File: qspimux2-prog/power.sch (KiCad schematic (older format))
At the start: 11 parts, among them Q601 BSS138, U601 MIC5504-3.3YM5, U602 AP2127K-ADJ

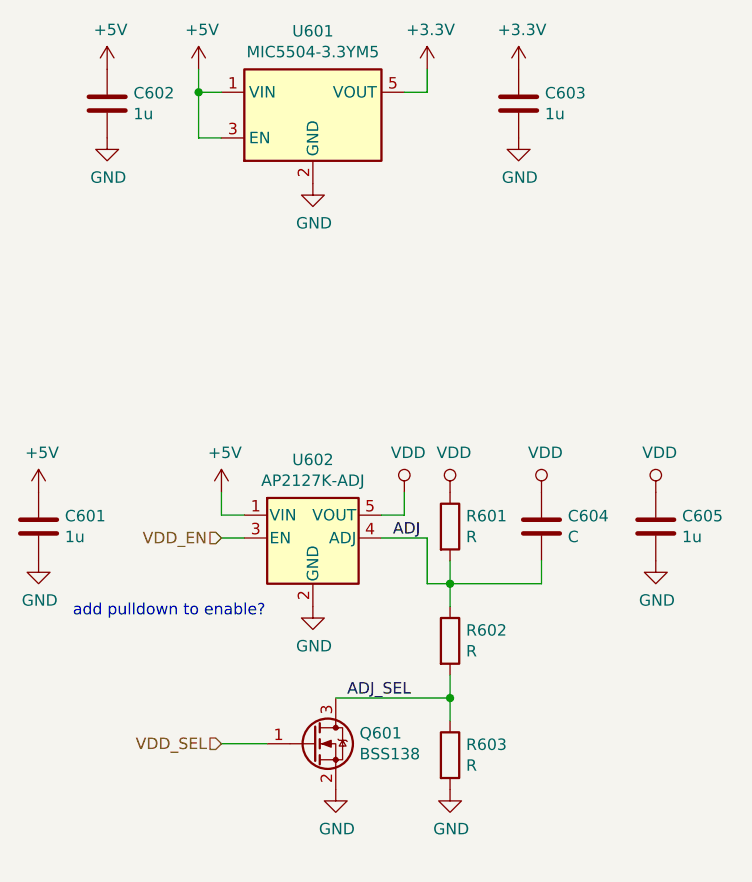
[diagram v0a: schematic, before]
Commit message: qspimux2-prog: add pull down resistors to enable and select inputs of vdd regulator
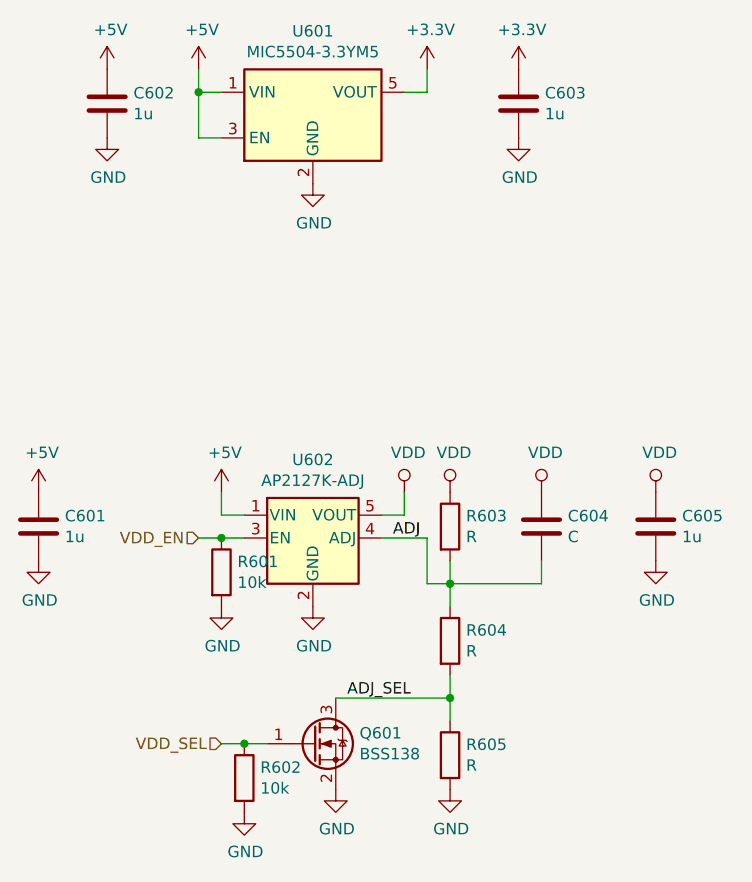
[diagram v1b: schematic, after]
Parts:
- added R601, R602: 10k, Resistor_SMD:R_0402_1005Metric, symbol Device:R
- renumbered R601 to R603, R602 to R604, R603 to R605
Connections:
- net GND: now also R601.2, R602.2
- net VDD_EN: now also R601.1
- net VDD_SEL: now also R602.1
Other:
- note removed: "add pulldown to enable?"
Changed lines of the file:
@@
 $EndComp
 $Comp
-L power:+3.3V #PWR0614
+L power:+3.3V #PWR0616
 U 1 1 5E022EF0
 P 3900 2550
-F 0 "#PWR0614" H 3900 2400 50  0001 C CNN
+F 0 "#PWR0616" H 3900 2400 50  0001 C CNN
 F 1 "+3.3V" H 3915 2723 50  0000 C CNN
 F 2 "" H 3900 2550 50  0001 C CNN
@@
 $EndComp
 $Comp
-L power:+3.3V #PWR0611
+L power:+3.3V #PWR0613
 U 1 1 5E0224B7
 P 3500 2550
-F 0 "#PWR0611" H 3500 2400 50  0001 C CNN
+F 0 "#PWR0613" H 3500 2400 50  0001 C CNN
 F 1 "+3.3V" H 3515 2723 50  0000 C CNN
 F 2 "" H 3500 2550 50  0001 C CNN
@@
 $EndComp
 $Comp
-L power:GND #PWR0607
+L power:GND #PWR0609
 U 1 1 5E020A11
 P 3000 3050
-F 0 "#PWR0607" H 3000 2800 50  0001 C CNN
+F 0 "#PWR0609" H 3000 2800 50  0001 C CNN
 F 1 "GND" H 3005 2877 50  0000 C CNN
 F 2 "" H 3000 3050 50  0001 C CNN
@@
 $EndComp
 $Comp
-L power:GND #PWR0615
+L power:GND #PWR0617
 U 1 1 5E021D81
 P 3900 2850
-F 0 "#PWR0615" H 3900 2600 50  0001 C CNN
+F 0 "#PWR0617" H 3900 2600 50  0001 C CNN
 F 1 "GND" H 3905 2677 50  0000 C CNN
 F 2 "" H 3900 2850 50  0001 C CNN
@@
 VDD_SEL
 $Comp
-L power:VDD #PWR0617
+L power:VDD #PWR0619
 U 1 1 5DF779E9
 P 4500 4400
-F 0 "#PWR0617" H 4500 4250 50  0001 C CNN
+F 0 "#PWR0619" H 4500 4250 50  0001 C CNN
 F 1 "VDD" H 4517 4573 50  0000 C CNN
 F 2 "" H 4500 4400 50  0001 C CNN
@@
 	1    0    0    -1
 $EndComp
-Text HLabel 2600 4600 0    50   Input ~ 0
+Text HLabel 2500 4600 0    50   Input ~ 0
 VDD_EN
 $Comp
-L power:GND #PWR0608
+L power:GND #PWR0610
 U 1 1 5DED5ED3
 P 3000 4900
-F 0 "#PWR0608" H 3000 4650 50  0001 C CNN
+F 0 "#PWR0610" H 3000 4650 50  0001 C CNN
 F 1 "GND" H 3005 4727 50  0000 C CNN
 F 2 "" H 3000 4900 50  0001 C CNN
@@
 $EndComp
 $Comp
-L power:GND #PWR0618
+L power:GND #PWR0620
 U 1 1 5DED62F9
 P 4500 4700
-F 0 "#PWR0618" H 4500 4450 50  0001 C CNN
+F 0 "#PWR0620" H 4500 4450 50  0001 C CNN
 F 1 "GND" H 4505 4527 50  0000 C CNN
 F 2 "" H 4500 4700 50  0001 C CNN
@@
 $EndComp
 $Comp
-L power:VDD #PWR0610
+L power:VDD #PWR0612
 U 1 1 5DED7A92
 P 3400 4400
-F 0 "#PWR0610" H 3400 4250 50  0001 C CNN
+F 0 "#PWR0612" H 3400 4250 50  0001 C CNN
 F 1 "VDD" H 3417 4573 50  0000 C CNN
 F 2 "" H 3400 4400 50  0001 C CNN
@@
 $EndComp
 $Comp
-L Device:R R601
+L Device:R R603
 U 1 1 5DEEFCBB
 P 3600 4550
-F 0 "R601" H 3670 4596 50  0000 L CNN
+F 0 "R603" H 3670 4596 50  0000 L CNN
 F 1 "R" H 3670 4505 50  0000 L CNN
 F 2 "Resistor_SMD:R_0402_1005Metric" V 3530 4550 50  0001 C CNN
@@
 $EndComp
 $Comp
-L Device:R R602
+L Device:R R604
 U 1 1 5DEF0794
 P 3600 5050
-F 0 "R602" H 3670 5096 50  0000 L CNN
+F 0 "R604" H 3670 5096 50  0000 L CNN
 F 1 "R" H 3670 5005 50  0000 L CNN
 F 2 "Resistor_SMD:R_0402_1005Metric" V 3530 5050 50  0001 C CNN
@@
 $EndComp
 $Comp
-L Device:R R603
+L Device:R R605
 U 1 1 5DEF5357
 P 3600 5550
-F 0 "R603" H 3670 5596 50  0000 L CNN
+F 0 "R605" H 3670 5596 50  0000 L CNN
 F 1 "R" H 3670 5505 50  0000 L CNN
 F 2 "Resistor_SMD:R_0402_1005Metric" V 3530 5550 50  0001 C CNN
@@
 $EndComp
 $Comp
-L power:GND #PWR0613
+L power:GND #PWR0615
 U 1 1 5DEF7FD0
 P 3600 5700
-F 0 "#PWR0613" H 3600 5450 50  0001 C CNN
+F 0 "#PWR0615" H 3600 5450 50  0001 C CNN
 F 1 "GND" H 3605 5527 50  0000 C CNN
 F 2 "" H 3600 5700 50  0001 C CNN
@@
 	3400 4500 3400 4400
 $Comp
-L power:VDD #PWR0612
+L power:VDD #PWR0614
 U 1 1 5DEFBE7B
 P 3600 4400
-F 0 "#PWR0612" H 3600 4250 50  0001 C CNN
+F 0 "#PWR0614" H 3600 4250 50  0001 C CNN
 F 1 "VDD" H 3617 4573 50  0000 C CNN
 F 2 "" H 3600 4400 50  0001 C CNN
@@
 	4000 4800 4000 4700
 $Comp
-L power:VDD #PWR0616
+L power:VDD #PWR0618
 U 1 1 5DF067EF
 P 4000 4400
-F 0 "#PWR0616" H 4000 4250 50  0001 C CNN
+F 0 "#PWR0618" H 4000 4250 50  0001 C CNN
 F 1 "VDD" H 4017 4573 50  0000 C CNN
 F 2 "" H 4000 4400 50  0001 C CNN
@@
 	3600 5300 3600 5200
 $Comp
-L power:GND #PWR0609
+L power:GND #PWR0611
 U 1 1 5DF0FC05
 P 3100 5700
-F 0 "#PWR0609" H 3100 5450 50  0001 C CNN
+F 0 "#PWR0611" H 3100 5450 50  0001 C CNN
 F 1 "GND" H 3105 5527 50  0000 C CNN
 F 2 "" H 3100 5700 50  0001 C CNN
@@
 ADJ_SEL
 Wire Wire Line
+	2500 4600 2600 4600
+Wire Wire Line
+	2600 5500 2700 5500
+$Comp
+L Device:R R602
+U 1 1 5DED3942
+P 2700 5650
+F 0 "R602" H 2770 5696 50  0000 L CNN
+F 1 "10k" H 2770 5605 50  0000 L CNN
+F 2 "Resistor_SMD:R_0402_1005Metric" V 2630 5650 50  0001 C CNN
+F 3 "~" H 2700 5650 50  0001 C CNN
+	1    2700 5650
+	1    0    0    -1
+$EndComp
+Connection ~ 2700 5500
+Wire Wire Line
+	2700 5500 2800 5500
+$Comp
+L power:GND #PWR0608
+U 1 1 5DEDC3EC
+P 2700 5800
+F 0 "#PWR0608" H 2700 5550 50  0001 C CNN
+F 1 "GND" H 2705 5627 50  0000 C CNN
+F 2 "" H 2700 5800 50  0001 C CNN
+F 3 "" H 2700 5800 50  0001 C CNN
+	1    2700 5800
+	1    0    0    -1
+$EndComp
+$Comp
+L Device:R R601
+U 1 1 5DEE2184
+P 2600 4750
+F 0 "R601" H 2670 4796 50  0000 L CNN
+F 1 "10k" H 2670 4705 50  0000 L CNN
+F 2 "Resistor_SMD:R_0402_1005Metric" V 2530 4750 50  0001 C CNN
+F 3 "~" H 2600 4750 50  0001 C CNN
+	1    2600 4750
+	1    0    0    -1
+$EndComp
+Connection ~ 2600 4600
+Wire Wire Line
 	2600 4600 2700 4600
-Text Notes 1950 4950 0    50   ~ 0
-add pulldown to enable?
-Wire Wire Line
-	2600 5500 2800 5500
+$Comp
+L power:GND #PWR0607
+U 1 1 5DEE6044
+P 2600 4900
+F 0 "#PWR0607" H 2600 4650 50  0001 C CNN
+F 1 "GND" H 2605 4727 50  0000 C CNN
+F 2 "" H 2600 4900 50  0001 C CNN
+F 3 "" H 2600 4900 50  0001 C CNN
+	1    2600 4900
+	1    0    0    -1
+$EndComp
 $EndSCHEMATC

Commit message: qspimux2-prog: add values for ldo feedback network
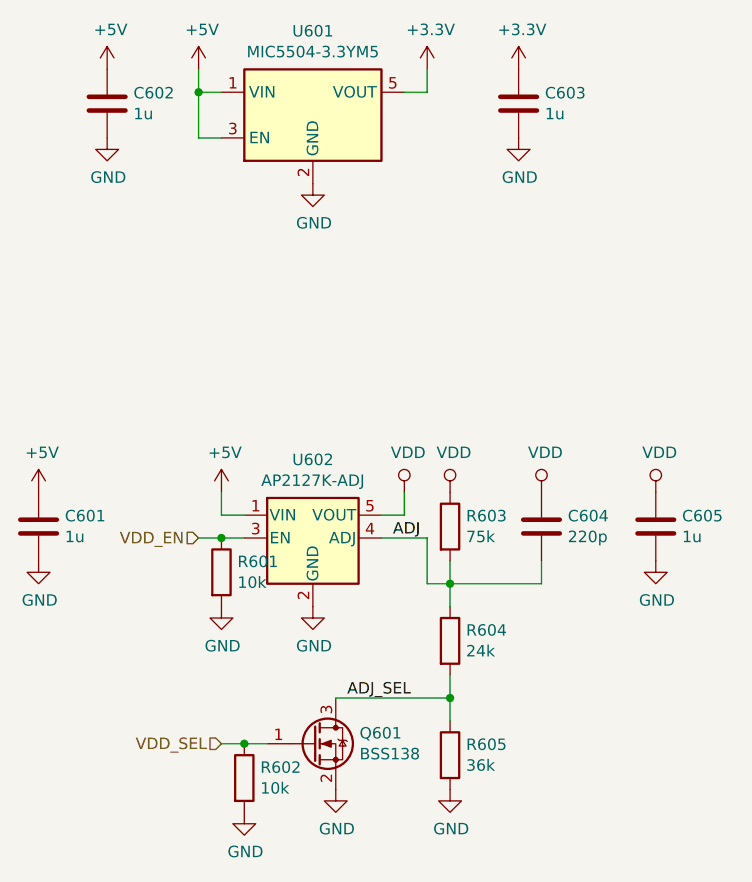
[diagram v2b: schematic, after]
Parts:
- C604: value C -> 220p
- R603: value R -> 75k
- R604: value R -> 24k
- R605: value R -> 36k
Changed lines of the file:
@@
 P 3600 4550
 F 0 "R603" H 3670 4596 50  0000 L CNN
-F 1 "R" H 3670 4505 50  0000 L CNN
+F 1 "75k" H 3670 4505 50  0000 L CNN
 F 2 "Resistor_SMD:R_0402_1005Metric" V 3530 4550 50  0001 C CNN
 F 3 "~" H 3600 4550 50  0001 C CNN
@@
 P 3600 5050
 F 0 "R604" H 3670 5096 50  0000 L CNN
-F 1 "R" H 3670 5005 50  0000 L CNN
+F 1 "24k" H 3670 5005 50  0000 L CNN
 F 2 "Resistor_SMD:R_0402_1005Metric" V 3530 5050 50  0001 C CNN
 F 3 "~" H 3600 5050 50  0001 C CNN
@@
 P 3600 5550
 F 0 "R605" H 3670 5596 50  0000 L CNN
-F 1 "R" H 3670 5505 50  0000 L CNN
+F 1 "36k" H 3670 5505 50  0000 L CNN
 F 2 "Resistor_SMD:R_0402_1005Metric" V 3530 5550 50  0001 C CNN
 F 3 "~" H 3600 5550 50  0001 C CNN
@@
 P 4000 4550
 F 0 "C604" H 4115 4596 50  0000 L CNN
-F 1 "C" H 4115 4505 50  0000 L CNN
+F 1 "220p" H 4115 4505 50  0000 L CNN
 F 2 "Capacitor_SMD:C_0402_1005Metric" H 4038 4400 50  0001 C CNN
 F 3 "~" H 4000 4550 50  0001 C CNN
